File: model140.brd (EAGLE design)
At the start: 100 x 96.5 mm, 17 parts

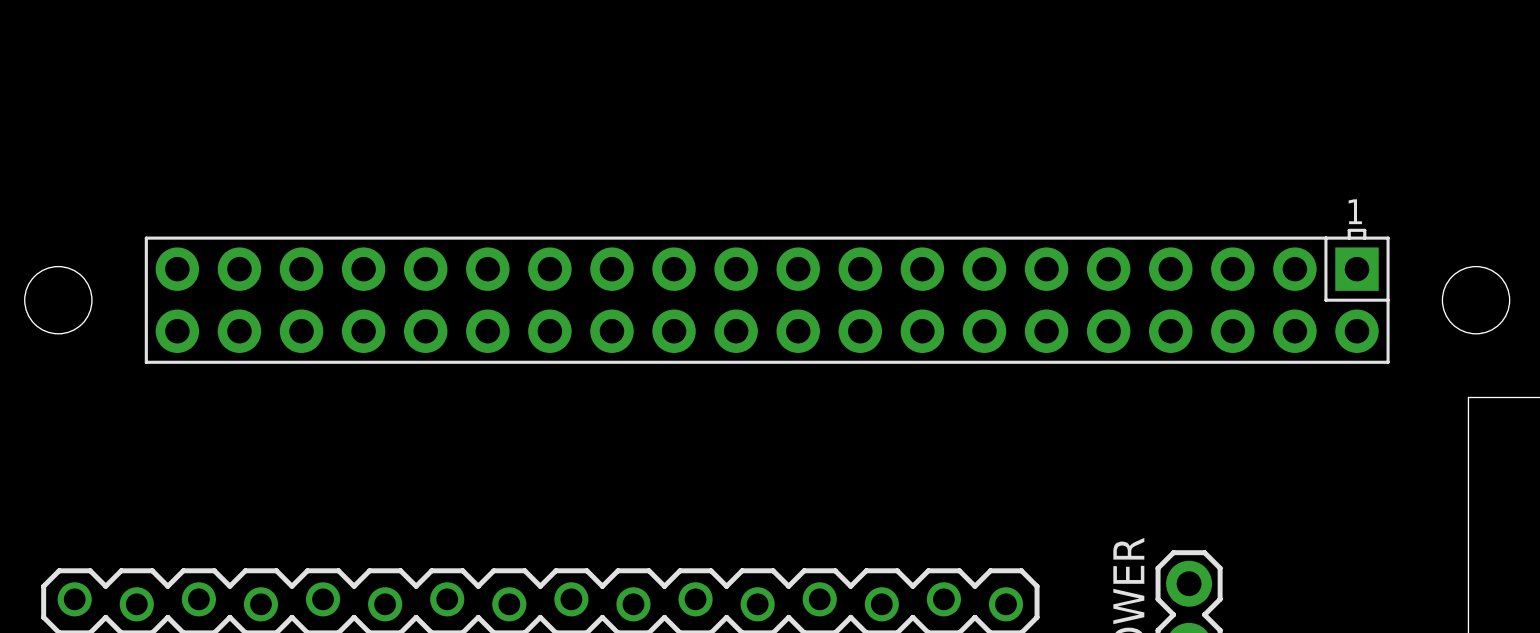
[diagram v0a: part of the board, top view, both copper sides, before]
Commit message: add pi-zero header duplicate
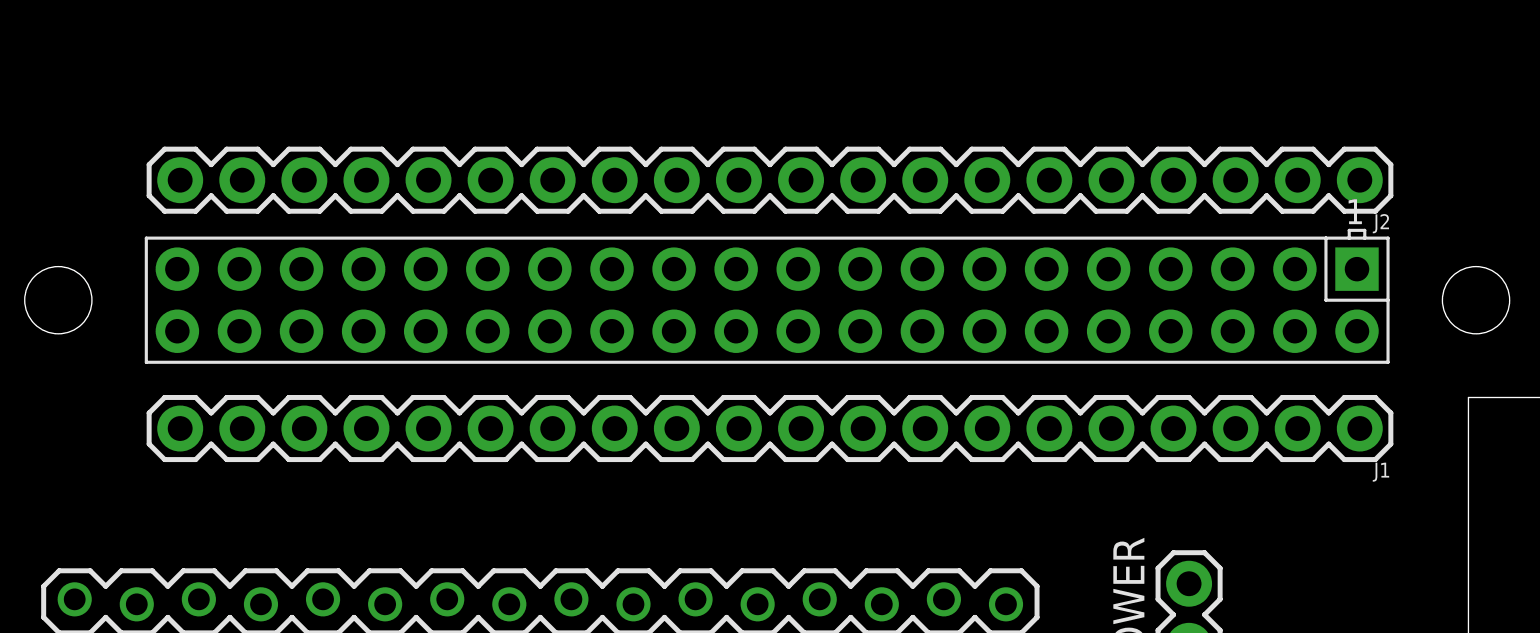
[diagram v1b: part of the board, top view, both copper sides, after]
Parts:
- added J1, J2: (no value), SparkFun-Connectors:1X20
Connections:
- new net 3V3@1: J2.1, U$1.1
- new net 3V3@2: J2.9, U$1.17
- new net N$1: J2.2, U$1.3
- new net N$10: J2.16, U$1.31
- new net N$11: J2.17, U$1.33
- new net N$12: J2.18, U$1.35
- new net N$13: J2.19, U$1.37
- new net N$14: J1.20, U$1.40
- new net N$15: J1.19, U$1.38
- new net N$16: J1.18, U$1.36
- new net N$17: J1.16, U$1.32
- new net N$18: J1.14, U$1.28
- new net N$19: J1.13, U$1.26
- new net N$2: J2.3, U$1.5
- new net N$20: J1.11, U$1.22
- new net N$21: J1.8, U$1.16
- new net N$22: J1.6, U$1.12
- new net N$3: J2.4, U$1.7
- new net N$4: J2.6, U$1.11
- new net N$5: J2.7, U$1.13
- new net N$6: J2.8, U$1.15
- new net N$7: J2.11, U$1.21
- new net N$8: J2.14, U$1.27
- new net N$9: J2.15, U$1.29
- net +5V: now also J1.1, J1.2
- net GND: now also J1.10, J1.15, J1.17, J1.3, J1.7, J2.13, J2.20, J2.5
- net SERIAL_RX: now also J1.5
- net SERIAL_TX: now also J1.4
- net SPI_CLK: now also J2.12
- net SPI_CS: now also J1.12
- net SPI_DC: now also J1.9
- net SPI_DI: now also J2.10
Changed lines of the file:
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@@
 <element name="U$1" library="rpi-zero" package="RASP_PI_ZERO_BOARD_FULL" value="RPI-ZERO" x="64.77" y="81.28" rot="R180"/>
 <element name="POWER" library="SparkFun-Connectors" package="1X02" value="" x="49.53" y="40.64" rot="R90"/>
+<element name="J1" library="SparkFun-Connectors" package="1X20" value="" x="56.515" y="49.53" rot="R180"/>
+<element name="J2" library="SparkFun-Connectors" package="1X20" value="" x="56.515" y="59.69" rot="R180"/>
 </elements>
 <signals>
@@
 <via x="6.35" y="92.71" extent="1-16" drill="5.08" diameter="2.54" shape="octagon"/>
 <via x="93.98" y="19.05" extent="1-16" drill="5.08" diameter="2.54" shape="octagon"/>
+<contactref element="J2" pad="5"/>
+<contactref element="J2" pad="13"/>
+<contactref element="J2" pad="20"/>
+<contactref element="J1" pad="17"/>
+<contactref element="J1" pad="15"/>
+<contactref element="J1" pad="10"/>
+<contactref element="J1" pad="7"/>
+<contactref element="J1" pad="3"/>
 </signal>
 <signal name="LCD_CS24">
@@
 <contactref element="U$1" pad="4"/>
 <contactref element="POWER" pad="1"/>
-<wire x1="55.88" y1="25.4" x2="98.27" y2="36.83" width="0" layer="19" extent="1-1"/>
+<contactref element="J1" pad="2"/>
+<contactref element="J1" pad="1"/>
+<wire x1="56.515" y1="49.53" x2="98.27" y2="36.83" width="0" layer="19" extent="1-1"/>
+<wire x1="53.975" y1="49.53" x2="56.515" y2="49.53" width="0" layer="19" extent="1-1"/>
+<wire x1="56.4" y1="53.51" x2="56.515" y2="49.53" width="0" layer="19" extent="1-1"/>
+<wire x1="53.86" y1="53.51" x2="56.4" y2="53.51" width="0" layer="19" extent="1-1"/>
+<wire x1="49.53" y1="40.64" x2="53.975" y2="49.53" width="0" layer="19" extent="1-1"/>
+<wire x1="55.88" y1="25.4" x2="49.53" y2="40.64" width="0" layer="19" extent="1-1"/>
 <wire x1="55.88" y1="21.59" x2="55.88" y2="25.4" width="0" layer="19" extent="1-1"/>
-<wire x1="49.53" y1="40.64" x2="55.88" y2="25.4" width="0" layer="19" extent="1-1"/>
-<wire x1="53.86" y1="53.51" x2="49.53" y2="40.64" width="0" layer="19" extent="1-1"/>
-<wire x1="56.4" y1="53.51" x2="53.86" y2="53.51" width="0" layer="19" extent="1-1"/>
 <wire x1="4.24" y1="30.4" x2="49.53" y2="40.64" width="0" layer="19" extent="1-1"/>
 </signal>
@@
 <contactref element="JP6" pad="12"/>
 <contactref element="U$1" pad="8"/>
-<wire x1="14.1" y1="24.7616" x2="48.78" y2="53.51" width="0" layer="19" extent="1-1"/>
+<contactref element="J1" pad="4"/>
+<wire x1="48.895" y1="49.53" x2="48.78" y2="53.51" width="0" layer="19" extent="1-1"/>
+<wire x1="14.1" y1="24.7616" x2="48.895" y2="49.53" width="0" layer="19" extent="1-1"/>
 </signal>
 <signal name="SERIAL_RX">
 <contactref element="U$1" pad="10"/>
 <contactref element="JP6" pad="11"/>
-<wire x1="16.64" y1="24.5584" x2="46.24" y2="53.51" width="0" layer="19" extent="1-1"/>
+<contactref element="J1" pad="5"/>
+<wire x1="46.355" y1="49.53" x2="46.24" y2="53.51" width="0" layer="19" extent="1-1"/>
+<wire x1="16.64" y1="24.5584" x2="46.355" y2="49.53" width="0" layer="19" extent="1-1"/>
 </signal>
 <signal name="SPI_CS">
 <contactref element="JP6" pad="14"/>
 <contactref element="U$1" pad="24"/>
-<wire x1="9.02" y1="24.7616" x2="28.46" y2="53.51" width="0" layer="19" extent="1-1"/>
+<contactref element="J1" pad="12"/>
+<wire x1="28.575" y1="49.53" x2="28.46" y2="53.51" width="0" layer="19" extent="1-1"/>
+<wire x1="9.02" y1="24.7616" x2="28.575" y2="49.53" width="0" layer="19" extent="1-1"/>
 </signal>
 <signal name="SPI_CLK">
 <contactref element="JP6" pad="15"/>
 <contactref element="U$1" pad="23"/>
+<contactref element="J2" pad="12"/>
+<wire x1="28.46" y1="56.05" x2="28.575" y2="59.69" width="0" layer="19" extent="1-1"/>
 <wire x1="6.48" y1="24.5584" x2="28.46" y2="56.05" width="0" layer="19" extent="1-1"/>
 </signal>
@@
 <contactref element="JP6" pad="16"/>
 <contactref element="U$1" pad="18"/>
-<wire x1="3.94" y1="24.7616" x2="36.08" y2="53.51" width="0" layer="19" extent="1-1"/>
+<contactref element="J1" pad="9"/>
+<wire x1="36.195" y1="49.53" x2="36.08" y2="53.51" width="0" layer="19" extent="1-1"/>
+<wire x1="3.94" y1="24.7616" x2="36.195" y2="49.53" width="0" layer="19" extent="1-1"/>
 </signal>
 <signal name="+3V3">
@@
 <contactref element="JP6" pad="13"/>
 <contactref element="U$1" pad="19"/>
+<contactref element="J2" pad="10"/>
+<wire x1="33.54" y1="56.05" x2="33.655" y2="59.69" width="0" layer="19" extent="1-1"/>
 <wire x1="11.56" y1="24.5584" x2="33.54" y2="56.05" width="0" layer="19" extent="1-1"/>
 </signal>
+<signal name="3V3@1">
+<contactref element="U$1" pad="1"/>
+<contactref element="J2" pad="1"/>
+<wire x1="56.4" y1="56.05" x2="56.515" y2="59.69" width="0" layer="19" extent="1-1"/>
+</signal>
+<signal name="N$1">
+<contactref element="U$1" pad="3"/>
+<contactref element="J2" pad="2"/>
+<wire x1="53.86" y1="56.05" x2="53.975" y2="59.69" width="0" layer="19" extent="1-1"/>
+</signal>
+<signal name="N$2">
+<contactref element="U$1" pad="5"/>
+<contactref element="J2" pad="3"/>
+<wire x1="51.32" y1="56.05" x2="51.435" y2="59.69" width="0" layer="19" extent="1-1"/>
+</signal>
+<signal name="N$3">
+<contactref element="U$1" pad="7"/>
+<contactref element="J2" pad="4"/>
+<wire x1="48.78" y1="56.05" x2="48.895" y2="59.69" width="0" layer="19" extent="1-1"/>
+</signal>
+<signal name="N$4">
+<contactref element="U$1" pad="11"/>
+<contactref element="J2" pad="6"/>
+<wire x1="43.7" y1="56.05" x2="43.815" y2="59.69" width="0" layer="19" extent="1-1"/>
+</signal>
+<signal name="N$5">
+<contactref element="U$1" pad="13"/>
+<contactref element="J2" pad="7"/>
+<wire x1="41.16" y1="56.05" x2="41.275" y2="59.69" width="0" layer="19" extent="1-1"/>
+</signal>
+<signal name="N$6">
+<contactref element="U$1" pad="15"/>
+<contactref element="J2" pad="8"/>
+<wire x1="38.62" y1="56.05" x2="38.735" y2="59.69" width="0" layer="19" extent="1-1"/>
+</signal>
+<signal name="3V3@2">
+<contactref element="U$1" pad="17"/>
+<contactref element="J2" pad="9"/>
+<wire x1="36.08" y1="56.05" x2="36.195" y2="59.69" width="0" layer="19" extent="1-1"/>
+</signal>
+<signal name="N$7">
+<contactref element="U$1" pad="21"/>
+<contactref element="J2" pad="11"/>
+<wire x1="31" y1="56.05" x2="31.115" y2="59.69" width="0" layer="19" extent="1-1"/>
+</signal>
+<signal name="N$8">
+<contactref element="U$1" pad="27"/>
+<contactref element="J2" pad="14"/>
+<wire x1="23.38" y1="56.05" x2="23.495" y2="59.69" width="0" layer="19" extent="1-1"/>
+</signal>
+<signal name="N$9">
+<contactref element="U$1" pad="29"/>
+<contactref element="J2" pad="15"/>
+<wire x1="20.84" y1="56.05" x2="20.955" y2="59.69" width="0" layer="19" extent="1-1"/>
+</signal>
+<signal name="N$10">
+<contactref element="U$1" pad="31"/>
+<contactref element="J2" pad="16"/>
+<wire x1="18.3" y1="56.05" x2="18.415" y2="59.69" width="0" layer="19" extent="1-1"/>
+</signal>
+<signal name="N$11">
+<contactref element="U$1" pad="33"/>
+<contactref element="J2" pad="17"/>
+<wire x1="15.76" y1="56.05" x2="15.875" y2="59.69" width="0" layer="19" extent="1-1"/>
+</signal>
+<signal name="N$12">
+<contactref element="U$1" pad="35"/>
+<contactref element="J2" pad="18"/>
+<wire x1="13.22" y1="56.05" x2="13.335" y2="59.69" width="0" layer="19" extent="1-1"/>
+</signal>
+<signal name="N$13">
+<contactref element="U$1" pad="37"/>
+<contactref element="J2" pad="19"/>
+<wire x1="10.68" y1="56.05" x2="10.795" y2="59.69" width="0" layer="19" extent="1-1"/>
+</signal>
+<signal name="N$14">
+<contactref element="U$1" pad="40"/>
+<contactref element="J1" pad="20"/>
+<wire x1="8.255" y1="49.53" x2="8.14" y2="53.51" width="0" layer="19" extent="1-1"/>
+</signal>
+<signal name="N$15">
+<contactref element="J1" pad="19"/>
+<contactref element="U$1" pad="38"/>
+<wire x1="10.795" y1="49.53" x2="10.68" y2="53.51" width="0" layer="19" extent="1-1"/>
+</signal>
+<signal name="N$16">
+<contactref element="U$1" pad="36"/>
+<contactref element="J1" pad="18"/>
+<wire x1="13.335" y1="49.53" x2="13.22" y2="53.51" width="0" layer="19" extent="1-1"/>
+</signal>
+<signal name="N$17">
+<contactref element="J1" pad="16"/>
+<contactref element="U$1" pad="32"/>
+<wire x1="18.415" y1="49.53" x2="18.3" y2="53.51" width="0" layer="19" extent="1-1"/>
+</signal>
+<signal name="N$18">
+<contactref element="J1" pad="14"/>
+<contactref element="U$1" pad="28"/>
+<wire x1="23.495" y1="49.53" x2="23.38" y2="53.51" width="0" layer="19" extent="1-1"/>
+</signal>
+<signal name="N$19">
+<contactref element="J1" pad="13"/>
+<contactref element="U$1" pad="26"/>
+<wire x1="26.035" y1="49.53" x2="25.92" y2="53.51" width="0" layer="19" extent="1-1"/>
+</signal>
+<signal name="N$20">
+<contactref element="J1" pad="11"/>
+<contactref element="U$1" pad="22"/>
+<wire x1="31.115" y1="49.53" x2="31" y2="53.51" width="0" layer="19" extent="1-1"/>
+</signal>
+<signal name="N$21">
+<contactref element="J1" pad="8"/>
+<contactref element="U$1" pad="16"/>
+<wire x1="38.735" y1="49.53" x2="38.62" y2="53.51" width="0" layer="19" extent="1-1"/>
+</signal>
+<signal name="N$22">
+<contactref element="J1" pad="6"/>
+<contactref element="U$1" pad="12"/>
+<wire x1="43.815" y1="49.53" x2="43.7" y2="53.51" width="0" layer="19" extent="1-1"/>
+</signal>
 </signals>

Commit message: as ordered
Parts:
- moved T4 10.5 mm to (69.8, 19.1), turned to 180 degrees
- moved T3 10.5 mm to (62.2, 19.1), turned to 180 degrees
- moved D1 7.73 mm to (80.0, 26.7)
- moved D2 7.73 mm to (80.0, 22.9)
- moved C2 7.62 mm to (69.8, 25.4)
- moved C1 7.62 mm to (62.2, 25.4)
- moved R1 6.48 mm to (52.1, 22.9)
- moved R2 6.48 mm to (52.1, 26.7)
- moved J6 2.54 mm to (4.24, 25.3)
- moved JP5 2.54 mm to (42.0, 39.9)
- moved JP6 2.54 mm to (42.0, 22.1)
- moved SV1 2.54 mm to (80.5, 33.0)
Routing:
- net +5V: track 0.00 -> 133.1 mm, vias 0 -> 1
- net LCD_CS1: track 0.00 -> 109.8 mm, vias 0 -> 3
- net PWM_NEGV: track 0.00 -> 107.2 mm
- net LCD_CS28: track 0.00 -> 104.1 mm, vias 0 -> 1
- net LCD_CS24: track 0.00 -> 99.9 mm, vias 0 -> 2
- net LCD_CS27: track 0.00 -> 98.5 mm, vias 0 -> 1
- net LCD_CS29: track 0.00 -> 97.7 mm, vias 0 -> 3
- net LCD_BZ: track 0.00 -> 95.5 mm, vias 0 -> 1
- net LCD_CS23: track 0.00 -> 92.5 mm, vias 0 -> 2
- net LCD_CS22: track 0.00 -> 87.9 mm, vias 0 -> 2
- net LCD_CS25: track 0.00 -> 87.2 mm, vias 0 -> 1
- net PWM_CONTRAST: track 0.00 -> 84.3 mm, vias 0 -> 1
- net LCD_CS26: track 0.00 -> 83.6 mm, vias 0 -> 1
- net LCD_E: track 0.00 -> 76.8 mm, vias 0 -> 3
- net LCD_CS20: track 0.00 -> 73.8 mm, vias 0 -> 1
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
